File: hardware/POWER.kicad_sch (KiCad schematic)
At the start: 65 parts, among them J4 532610371, SW1 TS-1010-C-A, U1 RT5750A, U13 XC6206P302MR, U2 RT9467, U3 RT4812, U5 RT6150, U6 RT5750A, U7 RT5750A

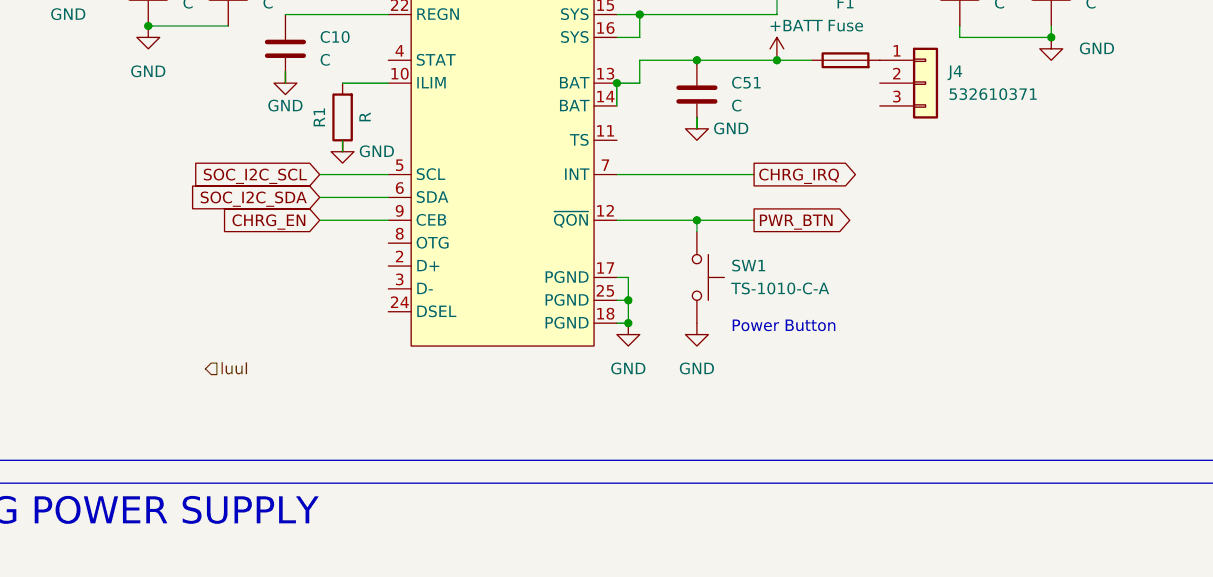
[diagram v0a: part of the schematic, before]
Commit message: added esd protection
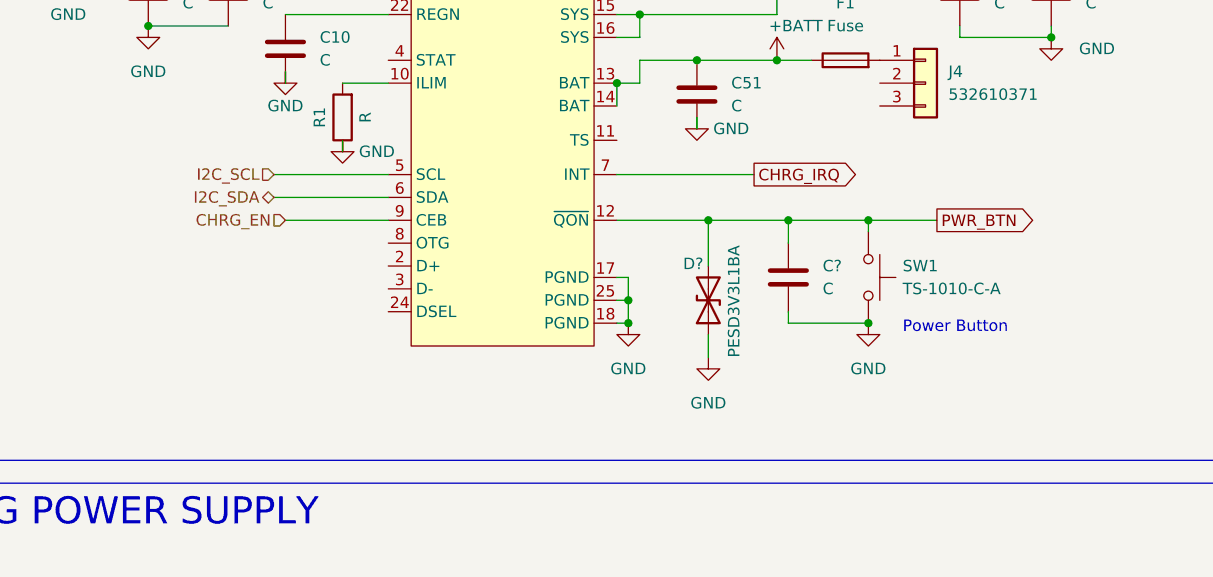
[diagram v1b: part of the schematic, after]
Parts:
- added C?: C, rlib_passive:C_0603_1608Metric, symbol rlib_passive:C
- added D?: PESD3V3L1BA, rlib_passive:D_SOD-323F, symbol rlib_passive:PESD3V3L1BA
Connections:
- net GND: now also C?.2, D?.1 (A1)
- net PWR_BTN: now also C?.1, D?.2 (A2)
- net SOC_I2C_SCL renamed I2C_SCL
- net SOC_I2C_SDA renamed I2C_SDA
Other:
- moved on the sheet: SW1
